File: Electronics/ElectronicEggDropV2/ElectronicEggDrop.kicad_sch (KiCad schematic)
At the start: 10 parts

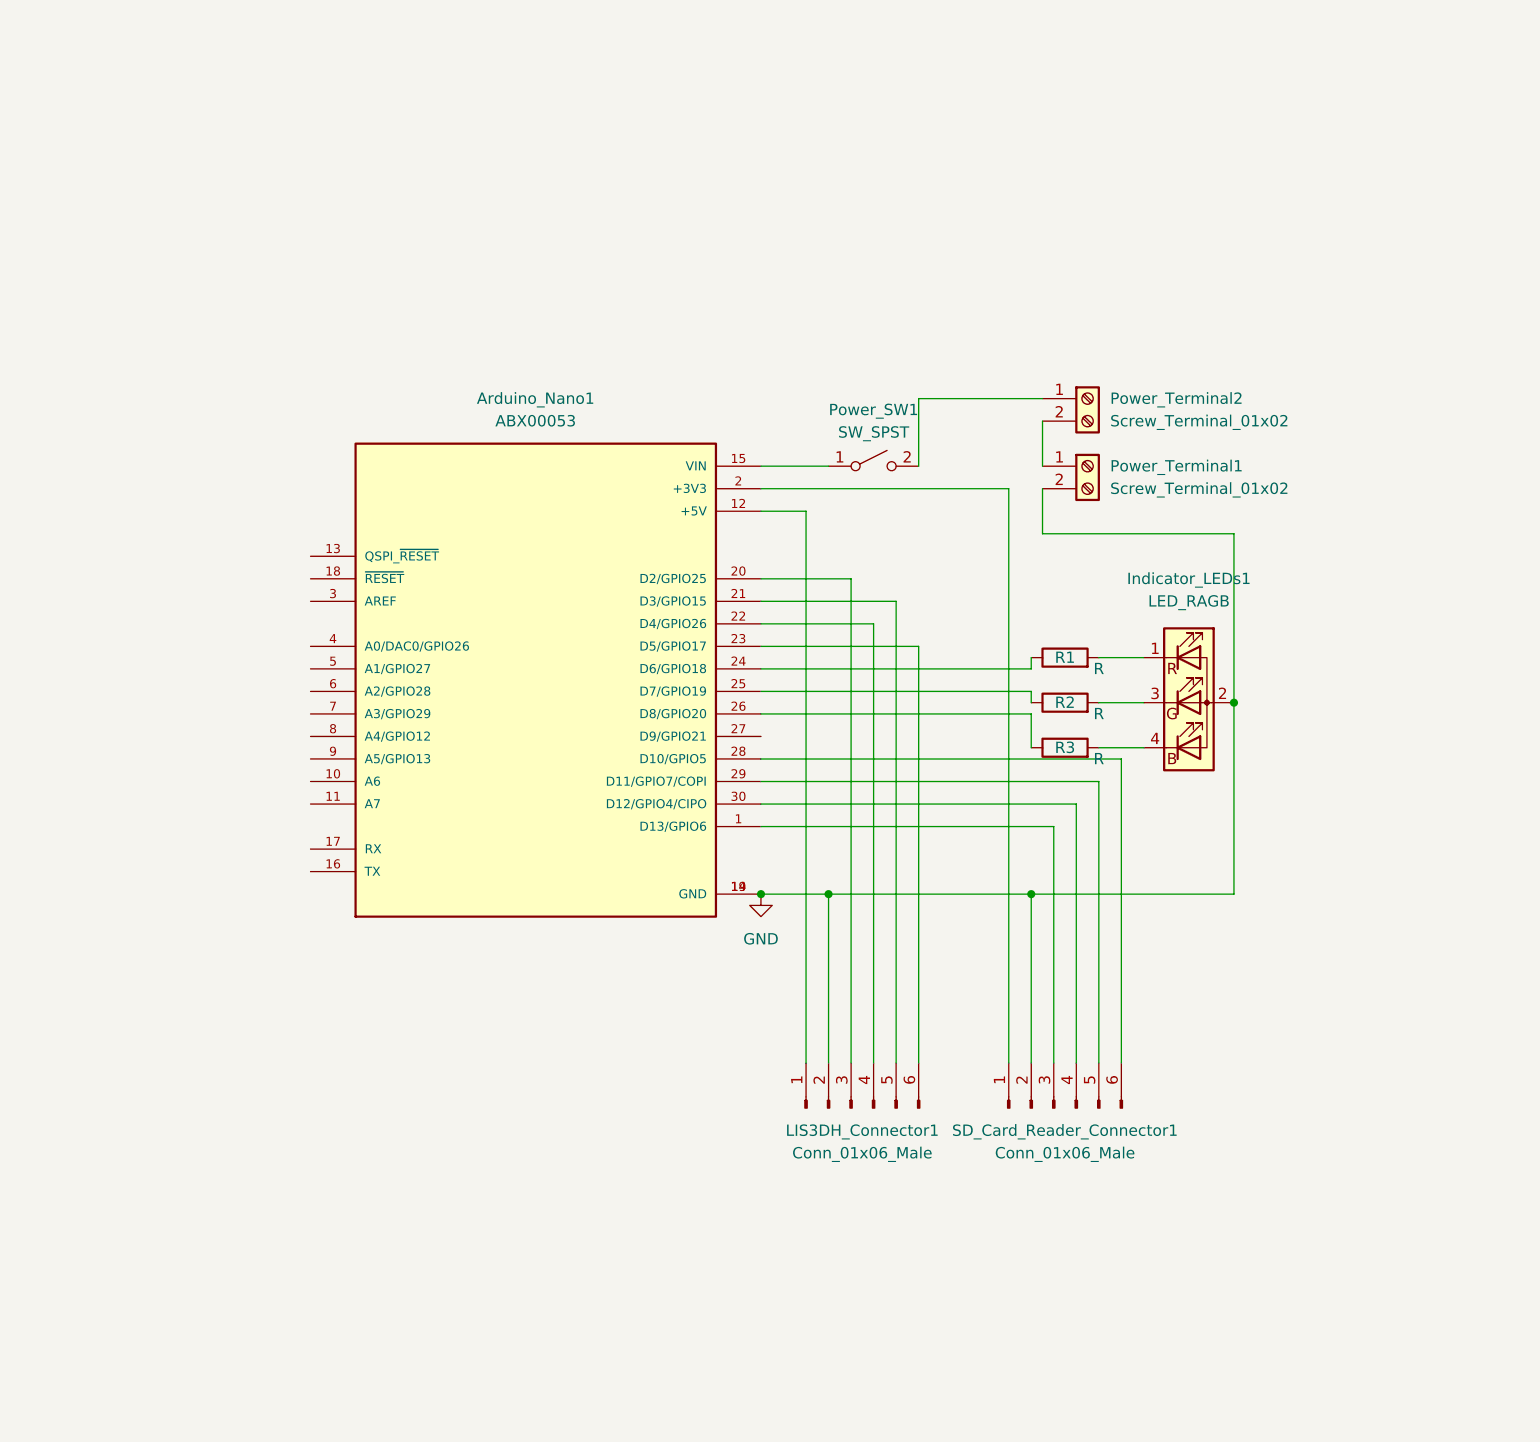
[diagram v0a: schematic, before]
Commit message: Updated v2, pretty much ready t order.  May experiment with reducing amountof spi wires used.
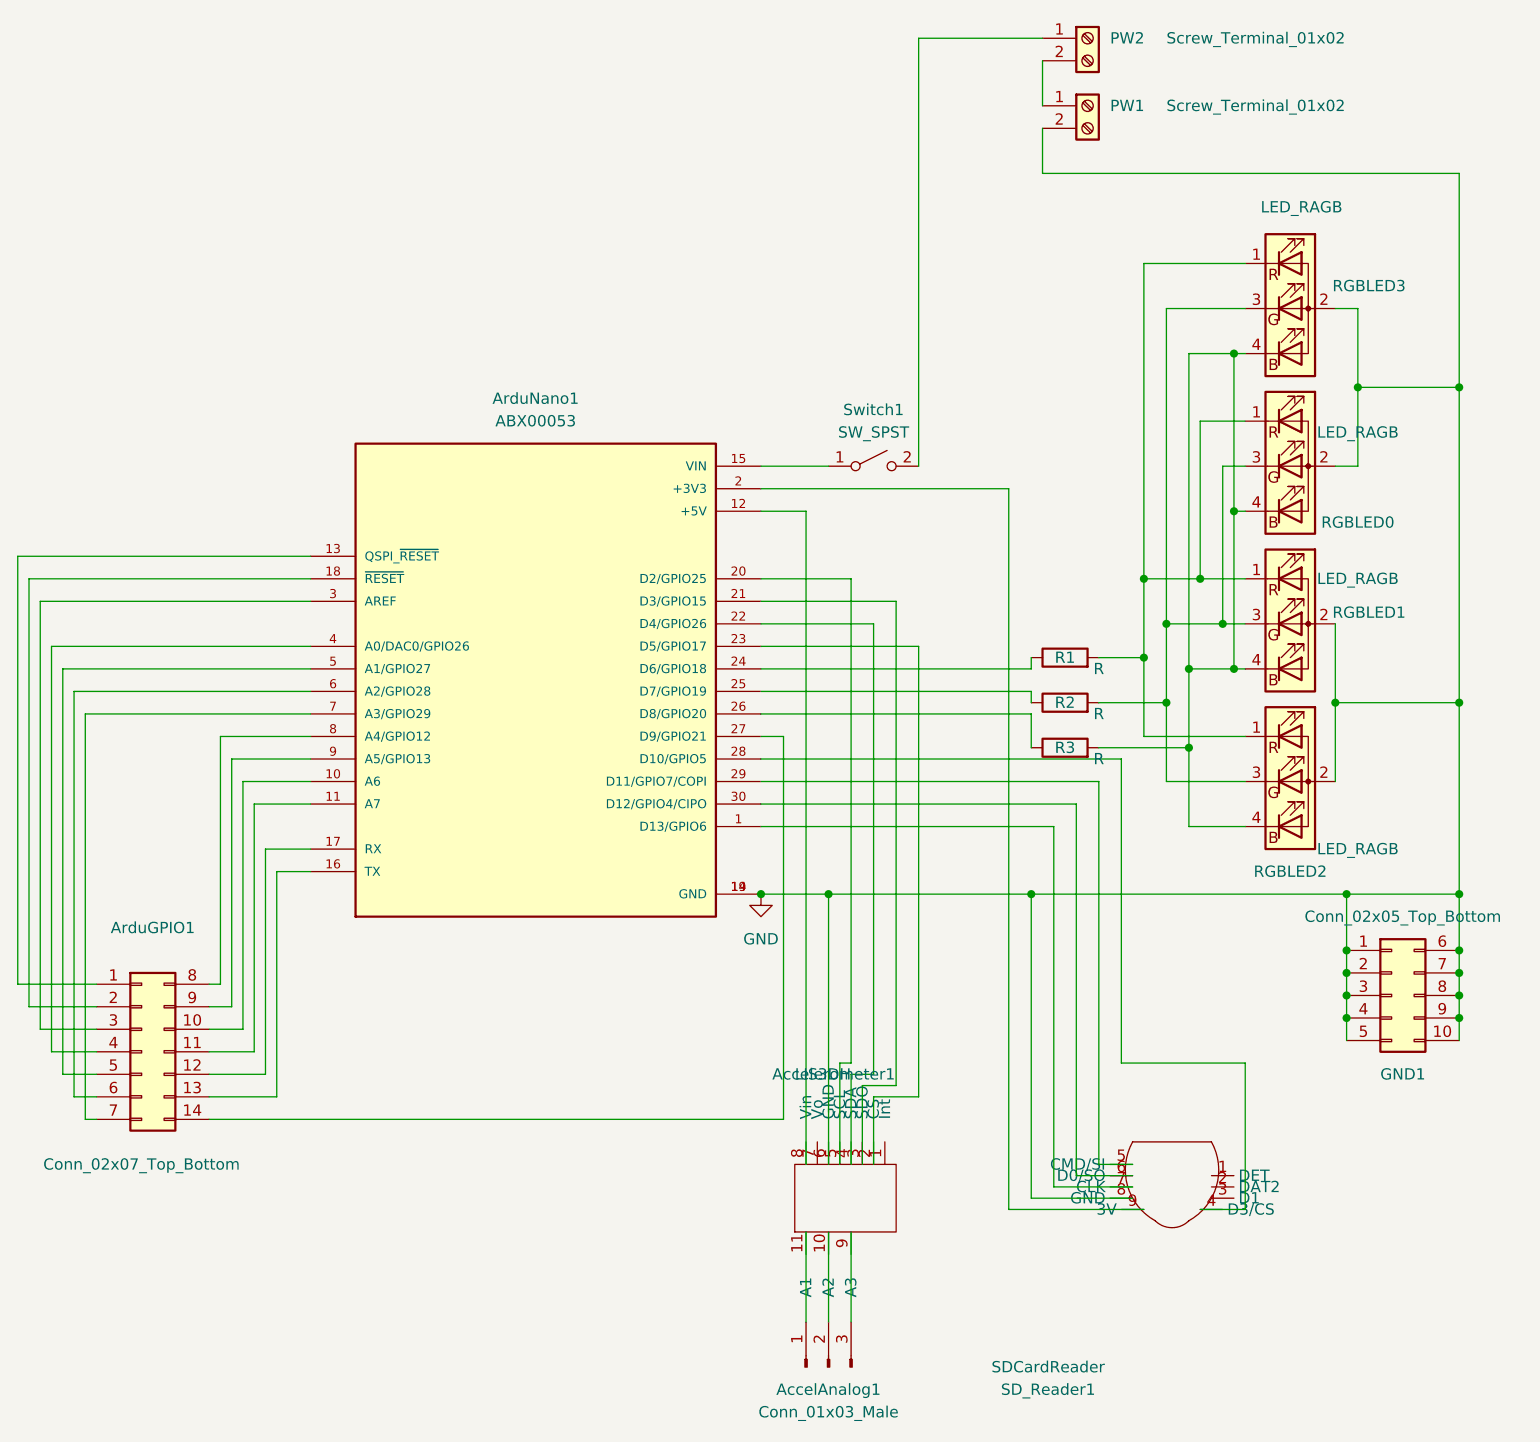
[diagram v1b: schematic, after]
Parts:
- removed LIS3DH_Connector1, SD_Card_Reader_Connector1: Conn_01x06_Male, Connector_PinSocket_2.54mm:PinSocket_1x06_P2.54mm_Vertical, symbol Connector:Conn_01x06_Male
- added AccelAnalog1: Conn_01x03_Male, Connector_PinHeader_2.54mm:PinHeader_1x03_P2.54mm_Vertical, symbol Connector:Conn_01x03_Male
- added Accelerometer1: LIS3DH, ElectronicEggDrop:LIS3DH, symbol ElectronicEggDrop:LIS3DH
- added ArduGPIO1: Conn_02x07_Top_Bottom, Connector_PinHeader_2.54mm:PinHeader_2x07_P2.54mm_Vertical, symbol Connector_Generic:Conn_02x07_Top_Bottom
- added GND1: Conn_02x05_Top_Bottom, Connector_PinHeader_2.54mm:PinHeader_2x05_P2.54mm_Vertical, symbol Connector_Generic:Conn_02x05_Top_Bottom
- added RGBLED0, RGBLED2, RGBLED3: LED_RAGB, Connector_PinSocket_2.54mm:PinSocket_1x04_P2.54mm_Vertical, symbol Device:LED_RAGB
- added SD_Reader1: SDCardReader, ElectronicEggDrop:SDCardReader, symbol ElectronicEggDrop:SDCardReader
- R1, R2, R3: footprint Resistor_THT:R_Axial_DIN0204_L3.6mm_D1.6mm_P5.08mm_Horizontal -> Resistor_THT:R_Axial_DIN0207_L6.3mm_D2.5mm_P7.62mm_Horizontal
- RGBLED1: renamed from Indicator_LEDs1; footprint Connector_PinSocket_2.54mm:PinSocket_2x03_P2.54mm_Vertical -> Connector_PinSocket_2.54mm:PinSocket_1x04_P2.54mm_Vertical
- Switch1: renamed from Power_SW1; footprint Connector_PinSocket_2.54mm:PinSocket_1x02_P2.54mm_Vertical -> Connector_PinSocket_2.54mm:PinSocket_1x03_P2.54mm_Vertical
- renumbered Arduino_Nano1 to ArduNano1, Power_Terminal1 to PW1, Power_Terminal2 to PW2
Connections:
- net GND: now also Accelerometer1.6 (GND), GND1.1 (Pin_1), GND1.10 (Pin_10), GND1.2 (Pin_2), GND1.3 (Pin_3), GND1.4 (Pin_4), GND1.5 (Pin_5), GND1.6 (Pin_6), GND1.7 (Pin_7), GND1.8 (Pin_8), GND1.9 (Pin_9), RGBLED0.2 (A), RGBLED2.2 (A), RGBLED3.2 (A), SD_Reader1.8 (GND)
- net at R3.2, RGBLED1.4 (BK): now also RGBLED0.4 (BK), RGBLED2.4 (BK), RGBLED3.4 (BK)
- net at R1.2, RGBLED1.1 (RK): now also RGBLED0.1 (RK), RGBLED2.1 (RK), RGBLED3.1 (RK)
- net at ArduNano1.12 (+5V): now also Accelerometer1.8 (Vin)
- net at ArduNano1.20 (D2/GPIO25): now also Accelerometer1.5 (SCL)
- net at ArduNano1.22 (D4/GPIO26): now also Accelerometer1.4 (SDA)
- net at ArduNano1.21 (D3/GPIO15): now also Accelerometer1.3 (SDO)
- net at ArduNano1.23 (D5/GPIO17): now also Accelerometer1.2 (CS)
- net at R2.2, RGBLED1.3 (GK): now also RGBLED0.3 (GK), RGBLED2.3 (GK), RGBLED3.3 (GK)
- net at ArduNano1.2 (+3V3): now also SD_Reader1.9 (3V)
- net at ArduNano1.1 (D13/GPIO6): now also SD_Reader1.7 (CLK)
- net at ArduNano1.30 (D12/GPIO4/CIPO): now also SD_Reader1.6 (D0/SO)
- net at ArduNano1.29 (D11/GPIO7/COPI): now also SD_Reader1.5 (CMD/SI)
- net at ArduNano1.28 (D10/GPIO5): now also SD_Reader1.4 (D3/CS)
- net at ArduNano1.10 (A6): now also ArduGPIO1.10 (Pin_10)
- net at ArduNano1.11 (A7): now also ArduGPIO1.11 (Pin_11)
- net at ArduNano1.13 (QSPI_~{RESET}): now also ArduGPIO1.1 (Pin_1)
- net at ArduNano1.16 (TX): now also ArduGPIO1.13 (Pin_13)
- net at ArduNano1.17 (RX): now also ArduGPIO1.12 (Pin_12)
- net at ArduNano1.18 (~{RESET}): now also ArduGPIO1.2 (Pin_2)
- net at ArduNano1.27 (D9/GPIO21): now also ArduGPIO1.14 (Pin_14)
- net at ArduNano1.3 (AREF): now also ArduGPIO1.3 (Pin_3)
- net at ArduNano1.4 (A0/DAC0/GPIO26): now also ArduGPIO1.4 (Pin_4)
- net at ArduNano1.5 (A1/GPIO27): now also ArduGPIO1.5 (Pin_5)
- net at ArduNano1.6 (A2/GPIO28): now also ArduGPIO1.6 (Pin_6)
- net at ArduNano1.7 (A3/GPIO29): now also ArduGPIO1.7 (Pin_7)
- net at ArduNano1.8 (A4/GPIO12): now also ArduGPIO1.8 (Pin_8)
- net at ArduNano1.9 (A5/GPIO13): now also ArduGPIO1.9 (Pin_9)
- new net: AccelAnalog1.2 (Pin_2), Accelerometer1.10 (A2)
- new net: AccelAnalog1.1 (Pin_1), Accelerometer1.11 (A1)
- new net: AccelAnalog1.3 (Pin_3), Accelerometer1.9 (A3)
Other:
- moved on the sheet: PW1, PW2, RGBLED1
